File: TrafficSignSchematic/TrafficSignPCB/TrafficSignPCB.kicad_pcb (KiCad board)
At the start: 2 copper layers, 196.9 x 129.5 mm, 25 parts, among them J1 IDC connector, J2 3.96mm pitch 4-pin polarized 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, U1 ATmega328P-PU, U2 SIM800L, Y1 16MHz

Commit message: Placed elements on PCB (Not final)
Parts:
- added J3: Power In, Connector_Molex:Molex_KK-396_A-41791-0004_1x04_P3.96mm_Vertical, F.Cu at (94.7, 65.0)
- R3, R4, R5: moved to B.Cu
- moved J2 140.6 mm to (54.0, 107.3), turned to 270 degrees
- moved VR2 135.2 mm to (66.5, 82.8), turned to 90 degrees
- moved CIN2 118.3 mm to (56.4, 82.3), turned to 180 degrees
- moved AE1 115.4 mm to (128.5, 150.4)
- moved L2 108.9 mm to (82.0, 87.5), turned to 90 degrees
- moved D2 101.2 mm to (73.2, 95.5), turned to 180 degrees
- moved L1 92.3 mm to (136.7, 84.8), turned to 90 degrees
- moved VR1 89.5 mm to (120.9, 85.3), turned to 90 degrees
- moved U1 86.8 mm to (80.8, 142.7), turned to 180 degrees
- moved Y1 80.9 mm to (86.9, 119.8)
- moved C1 77.7 mm to (86.9, 109.0), turned to 270 degrees
- moved U2 64.0 mm to (114.0, 117.3)
- moved COUT2 61.2 mm to (90.9, 79.9)
- moved CIN1 55.9 mm to (108.7, 80.3), turned to 180 degrees
- moved J1 50.9 mm to (54.6, 148.6), turned to 180 degrees
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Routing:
- net GND: track 0.00 -> 0.76 mm
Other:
- board size 196.9 x 129.5 mm -> 109.2 x 99.1 mm

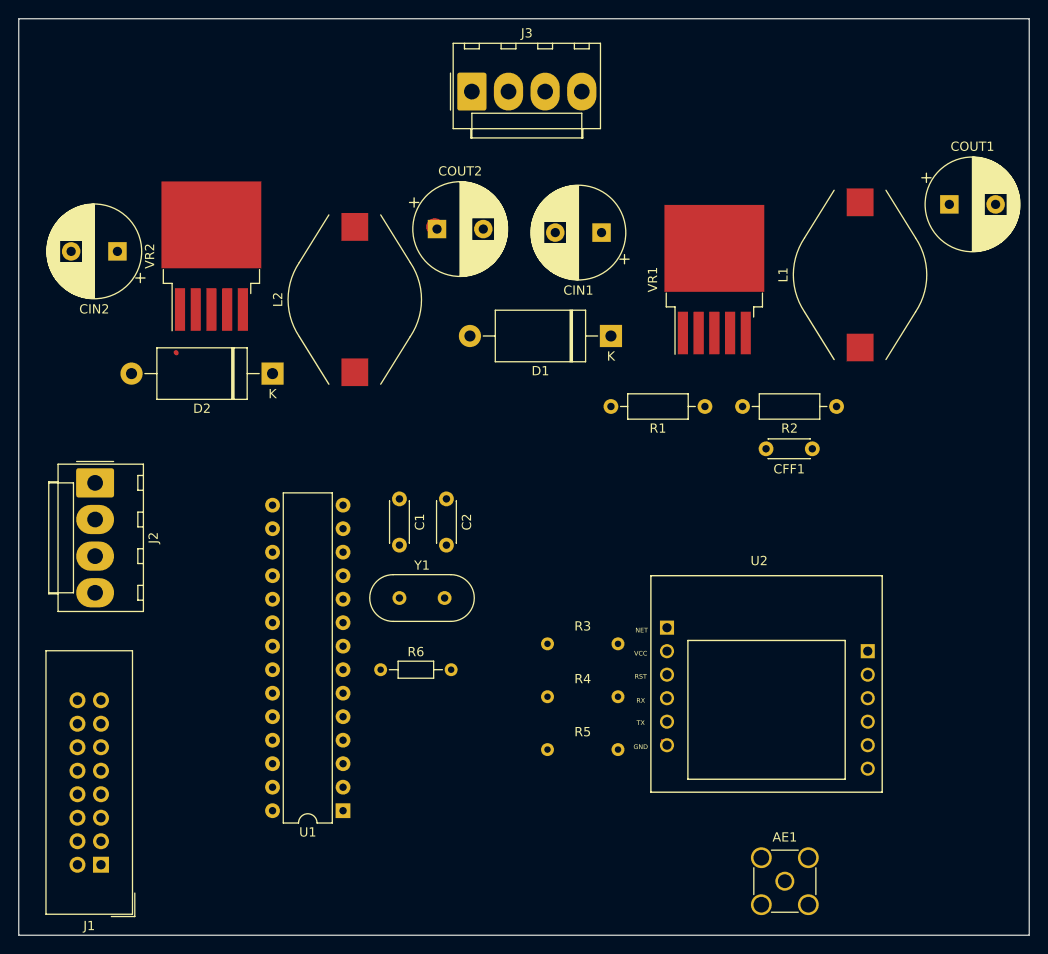
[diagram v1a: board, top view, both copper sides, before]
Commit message: Element placement v2
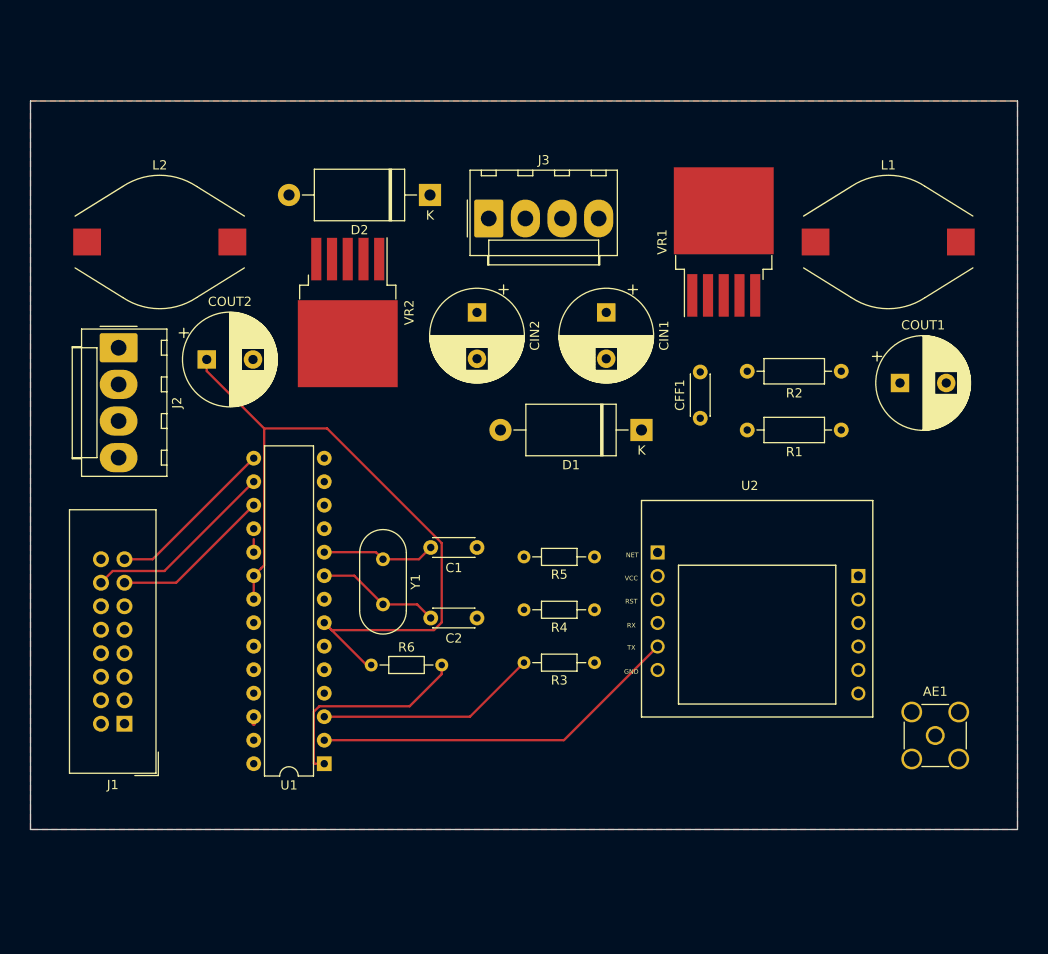
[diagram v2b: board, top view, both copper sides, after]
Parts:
- R3, R4, R5: moved to F.Cu
- moved CIN2 39.4 mm to (95.2, 88.9), turned to 270 degrees
- moved COUT2 28.6 mm to (66.0, 94.0)
- moved D2 25.7 mm to (90.2, 76.2)
- moved AE1 22.6 mm to (144.8, 134.6)
- moved L2 22.0 mm to (61.0, 81.3), turned to 0 degrees
- moved R5 21.0 mm to (100.3, 115.3)
- moved COUT1 20.0 mm to (141.0, 96.5)
- moved VR2 15.9 mm to (81.3, 88.9), turned to 270 degrees
- moved J1 15.5 mm to (57.1, 133.3)
- moved R1 14.9 mm to (134.6, 101.6)
- moved J2 14.8 mm to (56.5, 92.7)
- moved J3 13.8 mm to (96.5, 78.7)
- moved C2 13.3 mm to (95.2, 121.9), turned to 180 degrees
- moved CFF1 12.6 mm to (119.4, 100.3), turned to 90 degrees
- moved D1 10.7 mm to (113.0, 101.6)
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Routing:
- net +5V: track 0.33 -> 82.2 mm
- net /RXD: track 0.00 -> 40.2 mm
- net /TXD: track 0.00 -> 24.0 mm
- net Net-(R6-Pad2): track 0.00 -> 23.2 mm
- net STB: track 0.00 -> 21.0 mm
- net OE: track 0.00 -> 18.5 mm
- net CLK: track 0.00 -> 17.4 mm
- net Net-(C2-Pad2): track 0.00 -> 13.4 mm
- net Net-(C1-Pad2): track 0.00 -> 12.4 mm
- net /13: track 0.00 -> 1.41 mm
- net GND: track 0.76 -> 0.00 mm
- net D: track 0.00 -> 0.76 mm
- added copper zone on F.Cu, net GND
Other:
- board size 109.2 x 99.1 mm -> 106.7 x 78.7 mm

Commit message: Router IDC connector
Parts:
- removed J2: 3.96mm pitch 4-pin polarized connector, Connector_Molex:Molex_KK-396_A-41791-0004_1x04_P3.96mm_Vertical
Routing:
- net R1: track 0.00 -> 74.0 mm
- net G1: track 0.00 -> 65.7 mm
- net GND: track 0.00 -> 64.2 mm
- net B1: track 0.00 -> 60.2 mm
- net G0: track 0.00 -> 41.1 mm
- net B0: track 0.00 -> 38.2 mm
- net R0: track 0.00 -> 34.1 mm
- net D: track 0.76 -> 25.0 mm
- net C: track 0.00 -> 23.9 mm
- net A: track 0.00 -> 21.2 mm
- net +5V: track 82.2 -> 61.2 mm
- net B: track 0.00 -> 19.3 mm
- net Net-(R3-Pad2): track 0.00 -> 13.1 mm
- net Net-(R6-Pad2): track 23.2 -> 17.1 mm
- net Net-(R4-Pad2): track 0.00 -> 5.72 mm
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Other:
- net class Default: clearance 0.2 -> 0.2032
- rule trace_clearance: 0.2 -> 0.2032

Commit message: Router everything
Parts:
- added J2: 3.96mm pitch 4-pin polarized connector, Connector_Molex:Molex_KK-396_A-41791-0004_1x04_P3.96mm_Vertical, F.Cu at (56.6, 104.3)
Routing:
- net +4V: track 0.00 -> 81.5 mm
- net Net-(CFF1-Pad2): track 0.00 -> 64.0 mm
- net Net-(D2-Pad1): track 0.00 -> 53.6 mm
- net Net-(D1-Pad1): track 0.00 -> 51.3 mm
- net +12V: track 0.00 -> 51.0 mm
- net +5V: track 61.2 -> 106.5 mm
- net Net-(AE1-Pad1): track 0.00 -> 38.2 mm
- net G1: track 65.7 -> 62.1 mm
- net R1: track 74.0 -> 70.4 mm
- net B1: track 60.2 -> 56.9 mm
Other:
- rule trace_min: 0.2 -> 0.2032

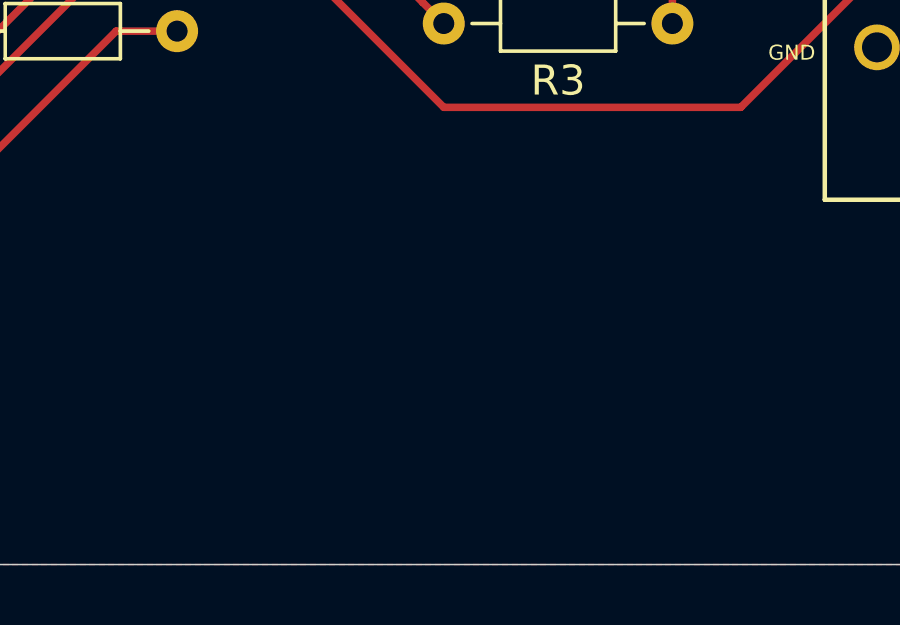
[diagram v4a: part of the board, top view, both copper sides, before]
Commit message: Added Elsys logo to PCB
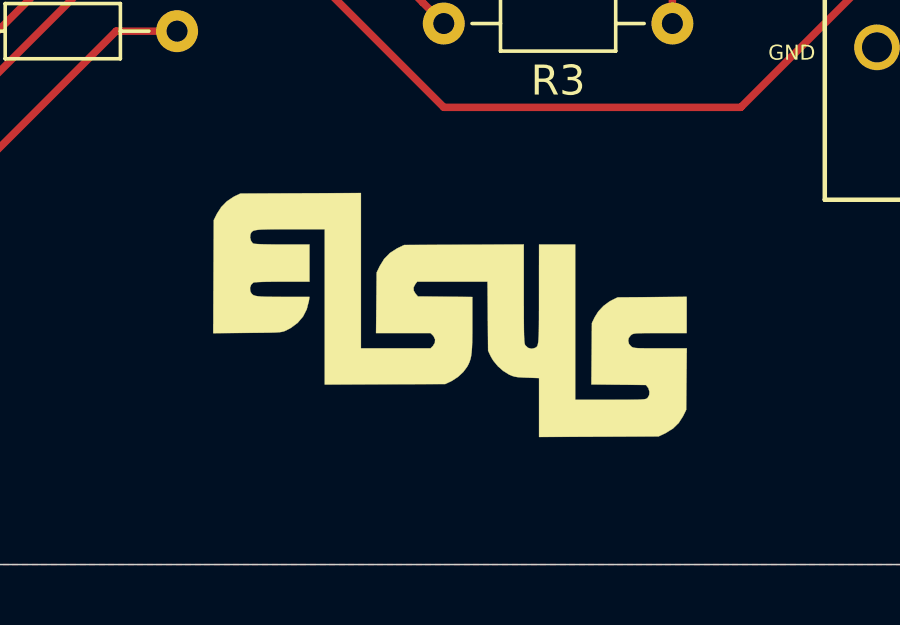
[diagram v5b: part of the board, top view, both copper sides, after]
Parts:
- added G***: LOGO, TrafficSignPCB:ElsysLogo, F.Cu at (100.6, 136.4)
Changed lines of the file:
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@@
     (tracks 242)
     (zones 0)
-    (modules 26)
+    (modules 27)
     (nets 41)
   )
@@
     (0 F.Cu signal)
     (31 B.Cu signal)
-    (32 B.Adhes user hide)
-    (33 F.Adhes user hide)
-    (34 B.Paste user hide)
-    (35 F.Paste user hide)
-    (36 B.SilkS user hide)
-    (37 F.SilkS user hide)
-    (38 B.Mask user hide)
-    (39 F.Mask user hide)
-    (40 Dwgs.User user hide)
-    (41 Cmts.User user hide)
-    (42 Eco1.User user hide)
-    (43 Eco2.User user hide)
-    (44 Edge.Cuts user hide)
-    (45 Margin user hide)
-    (46 B.CrtYd user hide)
-    (47 F.CrtYd user hide)
-    (48 B.Fab user hide)
-    (49 F.Fab user hide)
+    (32 B.Adhes user)
+    (33 F.Adhes user)
+    (34 B.Paste user)
+    (35 F.Paste user)
+    (36 B.SilkS user)
+    (37 F.SilkS user)
+    (38 B.Mask user)
+    (39 F.Mask user)
+    (40 Dwgs.User user)
+    (41 Cmts.User user)
+    (42 Eco1.User user)
+    (43 Eco2.User user)
+    (44 Edge.Cuts user)
+    (45 Margin user)
+    (46 B.CrtYd user)
+    (47 F.CrtYd user)
+    (48 B.Fab user)
+    (49 F.Fab user)
   )
   (setup
@@
     (add_net STB)
   )
+  (module TrafficSignPCB:ElsysLogo (layer F.Cu)
+    (at 100.584 136.398)
+    (fp_text reference G*** (at 0 0) (layer F.SilkS) hide
+      (effects (font (size 1.524 1.524) (thickness 0.3)))
+    )
+    (fp_text value LOGO (at 0.75 0) (layer F.SilkS) hide
+      (effects (font (size 1.524 1.524) (thickness 0.3)))
+    )
+    (fp_poly (pts (xy -3.01625 1.17475) (xy -0.695614 1.17475) (xy -0.617682 1.096818) (xy -0.551771 0.991905)
+      (xy -0.544501 0.877634) (xy -0.595874 0.769003) (xy -0.617682 0.744681) (xy -0.695614 0.66675)
+      (xy -2.512283 0.66675) (xy -2.502329 -0.341313) (xy -2.492375 -1.349375) (xy -2.391588 -1.562123)
+      (xy -2.242916 -1.804225) (xy -2.047721 -2.003736) (xy -1.809588 -2.157072) (xy -1.784373 -2.169338)
+      (xy -1.571625 -2.270125) (xy 0.420687 -2.279404) (xy 2.413 -2.288683) (xy 2.413 -0.643406)
+      (xy 2.413172 -0.273769) (xy 2.41379 0.037577) (xy 2.41501 0.295839) (xy 2.416985 0.506227)
+      (xy 2.419868 0.673948) (xy 2.423815 0.80421) (xy 2.42898 0.902221) (xy 2.435515 0.97319)
+      (xy 2.443576 1.022325) (xy 2.453317 1.054833) (xy 2.463829 1.074439) (xy 2.555269 1.158273)
+      (xy 2.666512 1.188155) (xy 2.751725 1.172715) (xy 2.787909 1.158988) (xy 2.818462 1.144164)
+      (xy 2.843864 1.123119) (xy 2.864592 1.090726) (xy 2.881127 1.04186) (xy 2.893948 0.971393)
+      (xy 2.903534 0.874202) (xy 2.910363 0.745158) (xy 2.914917 0.579137) (xy 2.917673 0.371013)
+      (xy 2.919111 0.115659) (xy 2.91971 -0.19205) (xy 2.919949 -0.557241) (xy 2.91999 -0.627063)
+      (xy 2.921 -2.286) (xy 4.1275 -2.286) (xy 4.1275 2.88925) (xy 5.30225 2.88925)
+      (xy 5.606652 2.889128) (xy 5.853913 2.888548) (xy 6.050393 2.887181) (xy 6.202449 2.884702)
+      (xy 6.316441 2.880786) (xy 6.398728 2.875106) (xy 6.455669 2.867335) (xy 6.493622 2.857148)
+      (xy 6.518947 2.844219) (xy 6.538002 2.828221) (xy 6.5405 2.82575) (xy 6.59158 2.734104)
+      (xy 6.600793 2.620101) (xy 6.567935 2.509306) (xy 6.543344 2.472079) (xy 6.482689 2.397125)
+      (xy 4.664763 2.378449) (xy 4.683125 0.333375) (xy 4.768474 0.151263) (xy 4.893803 -0.0511)
+      (xy 5.065754 -0.235589) (xy 5.26746 -0.385333) (xy 5.35028 -0.430543) (xy 5.540375 -0.523875)
+      (xy 6.691312 -0.533291) (xy 7.84225 -0.542707) (xy 7.84225 0.66675) (xy 6.95502 0.66675)
+      (xy 6.694754 0.666854) (xy 6.490374 0.667556) (xy 6.334265 0.669437) (xy 6.218814 0.673078)
+      (xy 6.136406 0.67906) (xy 6.079428 0.687965) (xy 6.040264 0.700375) (xy 6.0113 0.71687)
+      (xy 5.984923 0.738032) (xy 5.981353 0.7411) (xy 5.912258 0.828535) (xy 5.894916 0.92075)
+      (xy 5.917902 1.024695) (xy 5.981353 1.100399) (xy 6.007923 1.122182) (xy 6.036105 1.139231)
+      (xy 6.073503 1.152127) (xy 6.127725 1.161449) (xy 6.206375 1.167777) (xy 6.317061 1.171691)
+      (xy 6.467387 1.173772) (xy 6.66496 1.174598) (xy 6.917385 1.174749) (xy 6.956649 1.17475)
+      (xy 7.845508 1.17475) (xy 7.835941 2.199469) (xy 7.826375 3.224188) (xy 7.723189 3.433673)
+      (xy 7.579161 3.660121) (xy 7.388501 3.846596) (xy 7.147402 3.996729) (xy 7.117702 4.011151)
+      (xy 6.905625 4.111625) (xy 4.913312 4.120903) (xy 2.921 4.130182) (xy 2.921 2.166508)
+      (xy 2.516187 2.152846) (xy 2.341797 2.145716) (xy 2.214749 2.136159) (xy 2.118889 2.121325)
+      (xy 2.03806 2.098365) (xy 1.956107 2.064429) (xy 1.920875 2.047855) (xy 1.728233 1.928956)
+      (xy 1.546705 1.768682) (xy 1.394803 1.585482) (xy 1.308196 1.437267) (xy 1.222375 1.254125)
+      (xy 1.212626 0.103187) (xy 1.202877 -1.04775) (xy -1.138392 -1.04775) (xy -1.204196 -0.964094)
+      (xy -1.26133 -0.854255) (xy -1.255583 -0.746792) (xy -1.193416 -0.644708) (xy -1.116832 -0.555625)
+      (xy -0.209166 -0.546294) (xy 0.6985 -0.536962) (xy 0.6985 0.375723) (xy 0.69756 0.681006)
+      (xy 0.694071 0.930892) (xy 0.687028 1.133465) (xy 0.675425 1.29681) (xy 0.658257 1.42901)
+      (xy 0.634518 1.538149) (xy 0.603203 1.632312) (xy 0.563307 1.719584) (xy 0.522123 1.794)
+      (xy 0.392312 1.966911) (xy 0.219836 2.126687) (xy 0.025319 2.255014) (xy -0.02619 2.280907)
+      (xy -0.206375 2.365375) (xy -4.222751 2.382629) (xy -4.22275 -0.205686) (xy -4.22275 -2.794)
+      (xy -5.374561 -2.794001) (xy -5.690106 -2.793832) (xy -5.948289 -2.792782) (xy -6.155247 -2.790032)
+      (xy -6.317118 -2.784765) (xy -6.440038 -2.776162) (xy -6.530146 -2.763405) (xy -6.593579 -2.745677)
+      (xy -6.636475 -2.722159) (xy -6.66497 -2.692034) (xy -6.685203 -2.654484) (xy -6.700017 -2.617359)
+      (xy -6.710119 -2.521897) (xy -6.683987 -2.41924) (xy -6.630881 -2.337968) (xy -6.602748 -2.31708)
+      (xy -6.554822 -2.308299) (xy -6.450342 -2.300662) (xy -6.29625 -2.294391) (xy -6.099485 -2.289711)
+      (xy -5.866987 -2.286845) (xy -5.637713 -2.286) (xy -4.73075 -2.286) (xy -4.73075 -1.04775)
+      (xy -5.637713 -1.04775) (xy -5.888082 -1.046698) (xy -6.112689 -1.0437) (xy -6.30396 -1.038998)
+      (xy -6.45432 -1.032829) (xy -6.556197 -1.025436) (xy -6.601733 -1.017214) (xy -6.675052 -0.945559)
+      (xy -6.71179 -0.843003) (xy -6.704233 -0.735205) (xy -6.694182 -0.709739) (xy -6.668832 -0.662647)
+      (xy -6.638206 -0.625204) (xy -6.595235 -0.596302) (xy -6.532845 -0.574836) (xy -6.443967 -0.559697)
+      (xy -6.321529 -0.549778) (xy -6.15846 -0.543973) (xy -5.947687 -0.541174) (xy -5.68214 -0.540274)
+      (xy -5.611438 -0.540219) (xy -4.73 -0.53975) (xy -4.750546 -0.404813) (xy -4.822232 -0.126385)
+      (xy -4.946815 0.117076) (xy -5.123623 0.324697) (xy -5.351982 0.495606) (xy -5.508625 0.577954)
+      (xy -5.552261 0.597152) (xy -5.595709 0.612721) (xy -5.645987 0.62511) (xy -5.710111 0.634767)
+      (xy -5.795099 0.64214) (xy -5.907968 0.647678) (xy -6.055735 0.651828) (xy -6.245417 0.655039)
+      (xy -6.484031 0.657759) (xy -6.778595 0.660435) (xy -6.803405 0.660649) (xy -7.939434 0.670423)
+      (xy -7.93053 -1.213316) (xy -7.921625 -3.097056) (xy -7.818715 -3.30605) (xy -7.673909 -3.53221)
+      (xy -7.482377 -3.727401) (xy -7.258374 -3.877629) (xy -7.214174 -3.899534) (xy -7.032625 -3.984625)
+      (xy -5.024438 -3.993472) (xy -3.01625 -4.002318) (xy -3.01625 1.17475)) (layer F.SilkS) (width 0.01))
+  )
   (module Connector_IDC:IDC-Header_2x08_P2.54mm_Vertical (layer F.Cu)
